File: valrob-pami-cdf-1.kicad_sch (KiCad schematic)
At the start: 122 parts, among them J1 Conn_01x04, J2 USB_C_Receptacle_USB2.0_14P, J3 Conn_01x02, J4 Conn_01x04_Pin, J5 Conn_01x06, M1 Motor_Servo, Q1 Q_NMOS, Q2 Q_NMOS, Q3 Q_NMOS, SW1 SW_SPST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

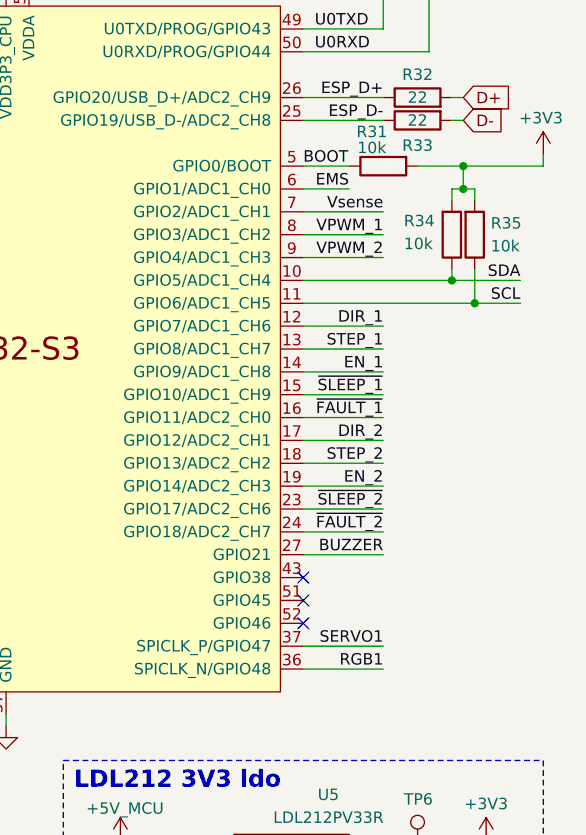
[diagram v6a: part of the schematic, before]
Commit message: schem/pcb: reorganize programmable gpios
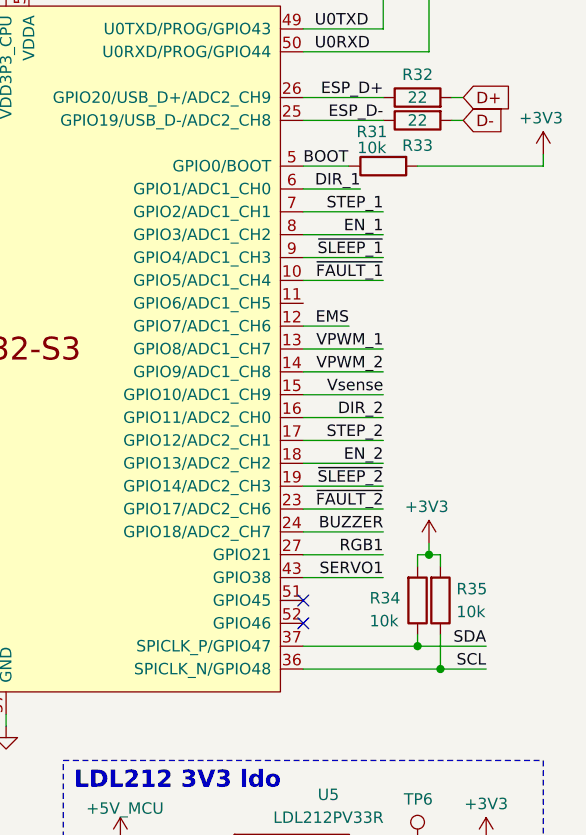
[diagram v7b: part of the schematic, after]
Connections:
- net BUZZER: now also U4.24 (GPIO18/ADC2_CH7); no longer U4.27 (GPIO21)
- net DIR_1: now also U4.6 (GPIO1/ADC1_CH0); no longer U4.12 (GPIO7/ADC1_CH6)
- net DIR_2: now also U4.16 (GPIO11/ADC2_CH0); no longer U4.17 (GPIO12/ADC2_CH1)
- net EMS: now also U4.12 (GPIO7/ADC1_CH6); no longer U4.6 (GPIO1/ADC1_CH0)
- net EN_1: now also U4.8 (GPIO3/ADC1_CH2); no longer U4.14 (GPIO9/ADC1_CH8)
- net EN_2: now also U4.18 (GPIO13/ADC2_CH2); no longer U4.19 (GPIO14/ADC2_CH3)
- net RGB1: now also U4.27 (GPIO21); no longer U4.36 (SPICLK_N/GPIO48)
- net SCL: now also U4.36 (SPICLK_N/GPIO48); no longer U4.11 (GPIO6/ADC1_CH5)
- net SDA: now also U4.37 (SPICLK_P/GPIO47); no longer U4.10 (GPIO5/ADC1_CH4)
- net SERVO1: now also U4.43 (GPIO38); no longer U4.37 (SPICLK_P/GPIO47)
- net STEP_1: now also U4.7 (GPIO2/ADC1_CH1); no longer U4.13 (GPIO8/ADC1_CH7)
- net STEP_2: now also U4.17 (GPIO12/ADC2_CH1); no longer U4.18 (GPIO13/ADC2_CH2)
- net VPWM_1: now also U4.13 (GPIO8/ADC1_CH7); no longer U4.8 (GPIO3/ADC1_CH2)
- net VPWM_2: now also U4.14 (GPIO9/ADC1_CH8); no longer U4.9 (GPIO4/ADC1_CH3)
- net Vsense: now also U4.15 (GPIO10/ADC1_CH9); no longer U4.7 (GPIO2/ADC1_CH1)
- net ~{FAULT_1}: now also U4.10 (GPIO5/ADC1_CH4); no longer U4.16 (GPIO11/ADC2_CH0)
- net ~{FAULT_2}: now also U4.23 (GPIO17/ADC2_CH6); no longer U4.24 (GPIO18/ADC2_CH7)
- net ~{SLEEP_1}: now also U4.9 (GPIO4/ADC1_CH3); no longer U4.15 (GPIO10/ADC1_CH9)
- net ~{SLEEP_2}: now also U4.19 (GPIO14/ADC2_CH3); no longer U4.23 (GPIO17/ADC2_CH6)
- no-connect marks 20 -> 19
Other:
- moved on the sheet: R34, R35

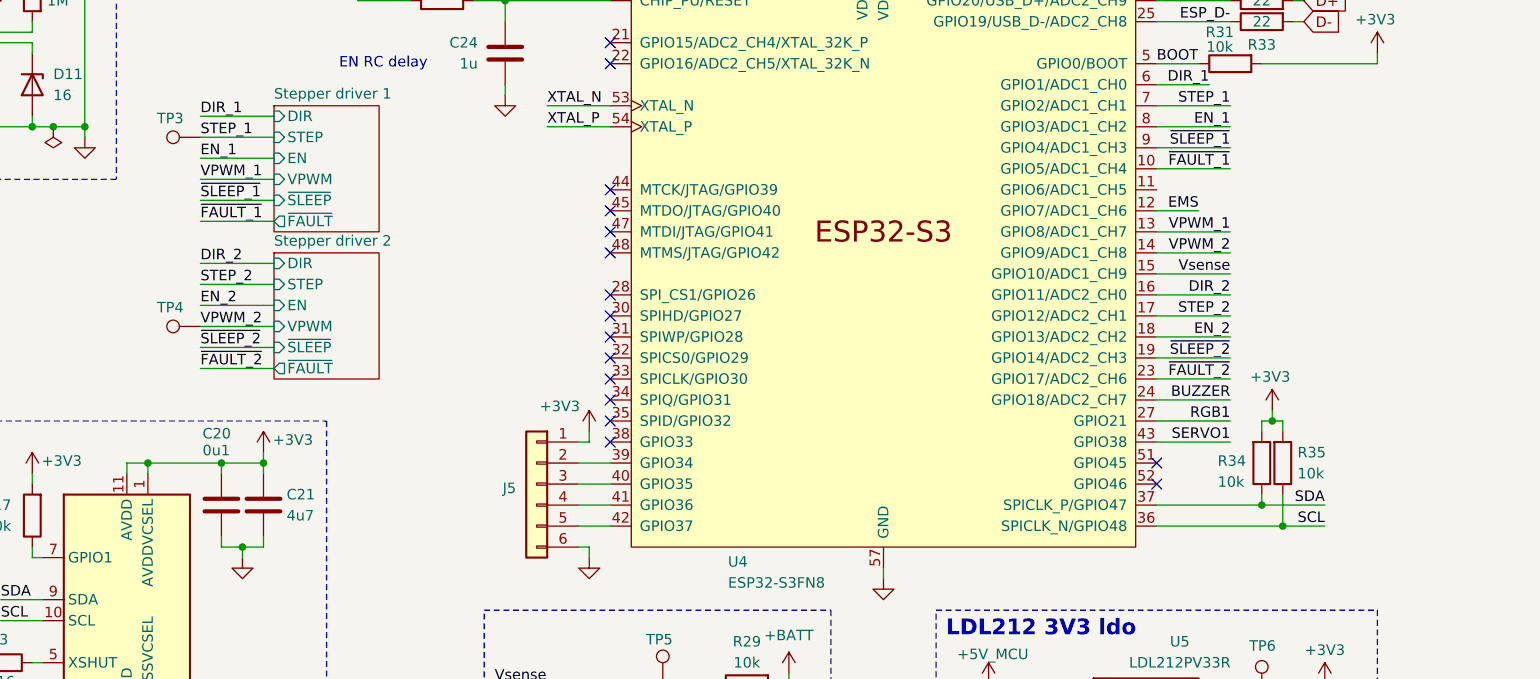
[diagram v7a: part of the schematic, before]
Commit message: pcb: add local stepper drivers routing
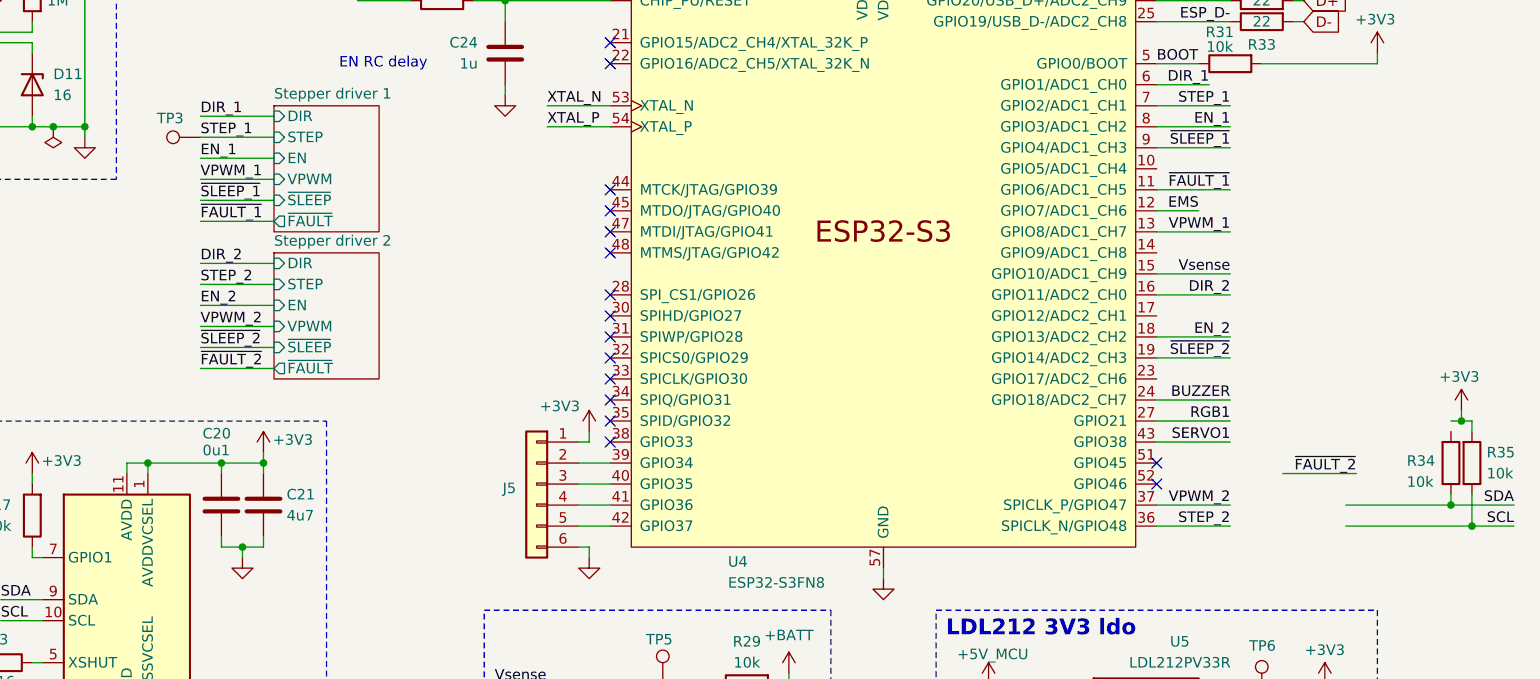
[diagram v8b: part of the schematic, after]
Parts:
- removed TP4: TestPoint, TestPoint:TestPoint_Pad_D2.0mm, symbol Connector:TestPoint
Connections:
- net +3V3: no longer R34.2
- net SCL: no longer U4.36 (SPICLK_N/GPIO48)
- net SDA: no longer U4.37 (SPICLK_P/GPIO47)
- net STEP_2: now also U4.36 (SPICLK_N/GPIO48); no longer U4.17 (GPIO12/ADC2_CH1)
- net VPWM_2: now also U4.37 (SPICLK_P/GPIO47); no longer U4.14 (GPIO9/ADC1_CH8)
- net ~{FAULT_1}: now also U4.11 (GPIO6/ADC1_CH5); no longer U4.10 (GPIO5/ADC1_CH4)
- net ~{FAULT_2}: no longer U4.23 (GPIO17/ADC2_CH6)
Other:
- moved on the sheet: R34, R35
